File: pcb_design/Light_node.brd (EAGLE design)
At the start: 17.8 x 37.3 mm, 29 parts, among them IC1 ATmega328P, IC2 MIC5225-5v, Q1 reset, Y1 16MHz

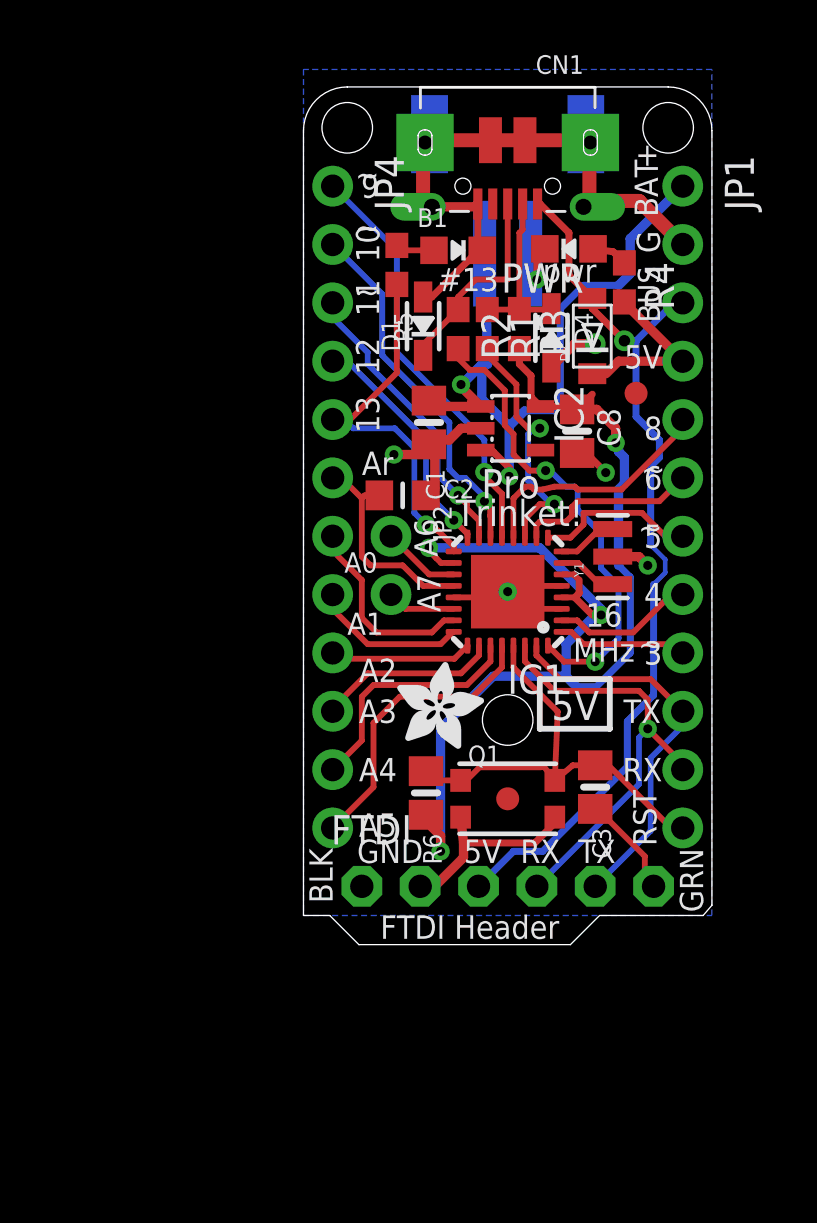
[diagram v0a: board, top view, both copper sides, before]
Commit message: Pulled the regulator components
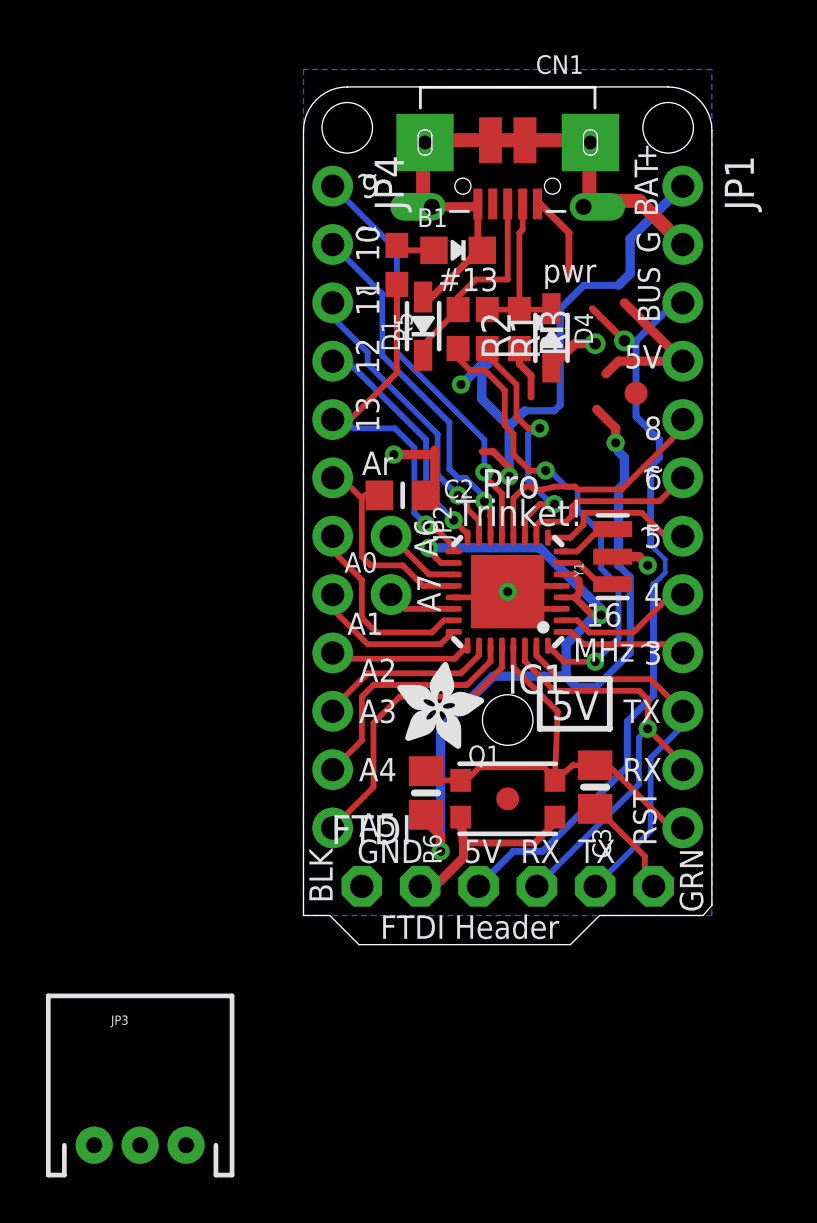
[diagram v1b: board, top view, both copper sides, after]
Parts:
- removed BAT: JST 2-PH, microbuilder:JSTPH2
- removed C1, C8: 10uF, microbuilder:0805-NO
- removed D2: SCHOTTKY, adafruit:SOD-123FL
- removed IC2: MIC5225-5v, adafruit:SOT23-5L
- removed PWR: green, microbuilder:CHIPLED_0805_NOOUTLINE
- removed R4: 470 (0603), microbuilder:0603-NO
- added JP3: (no value), SparkFun:JST-3-PTH
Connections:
- removed net N$6: PWR.A, R4.1
- net +5V: no longer C8.1, D2.C, IC2.5, R4.2
- net GND: no longer BAT.1, C1.2, C8.2, IC2.2, PWR.C
- net VBAT: no longer BAT.2, C1.1, IC2.1, IC2.3
- net VBUS: no longer D2.A
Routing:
- net VBAT: track 32.7 -> 24.3 mm
- net GND: track 58.0 -> 50.0 mm, vias 6 -> 4
- net +5V: track 60.2 -> 55.8 mm
- net VBUS: track 39.5 -> 37.6 mm
- net N$6: track 1.57 -> 0.00 mm

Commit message: added a bunch of new stuff in
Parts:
- removed JP2: (no value), microbuilder:1X02_ROUND
- removed JP4: (no value), adafruit:1X12-CB
- added B2: red, microbuilder:CHIPLED_0805_NOOUTLINE
- added C1, C4: 10µF, microbuilder:0805-NO
- added C5, C8: 10uF, microbuilder:0805-NO
- added CN2: JSTPH, microbuilder:JSTPH2
- added D2, D3: SCHOTTKY, adafruit:SOD-123FL
- added IC2: MIC5225-3.3v, adafruit:SOT23-5L
- added LED2: GREEN, microbuilder:CHIPLED_0805_NOOUTLINE
- added R4: 470 (0603), microbuilder:0603-NO
- added R8: 470, microbuilder:0805-NO
- added R9: 10K\, microbuilder:0805-NO
- added U1: MCP73831T-2ACI/OT, microbuilder:SOT23-5
- JP1: device adafruit:1X12-CB -> microbuilder:1X02_ROUND
- moved JP3 43.0 mm to (26.0, 4.00), turned to 180 degrees
- moved JP1 34.7 mm to (19.0, -15.0), turned to 0 degrees
- moved D4 12.0 mm to (13.7, 27.1)
- moved R3 11.8 mm to (12.1, 27.5)
- moved R1 11.7 mm to (10.6, 27.5)
- moved IC1 11.2 mm to (11.0, 16.1)
- moved U$7 11.2 mm to (6.17, 9.24)
- moved B1 11.2 mm to (8.84, 31.0)
- moved C3 11.2 mm to (14.8, 7.59)
- moved CN1 11.2 mm to (11.0, 33.8)
- moved FTDI 11.2 mm to (11.0, 3.27)
- moved Q1 11.2 mm to (11.0, 7.08)
- moved R2 11.2 mm to (8.84, 27.5)
- moved R6 11.2 mm to (7.44, 7.33)
- moved U$1 11.2 mm to (16.6, 24.7)
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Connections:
- new net +3V3: C8.1, IC2.5
- new net N$10: IC1.4, IC1.6
- new net N$4: B2.A, R4.1
- new net N$5: IC1.18
- new net N$6: R8.2, U1.1
- new net N$7: R9.1, U1.5
- new net N$8: LED2.A, R8.1
- new net N$9: C5.1, D2.C, D3.C, IC2.1, IC2.3
- new net STRIP_CNTRL: JP3.2
- net +5V: now also C1.1, CN1.VBUS, D2.A, JP1.1, R4.2, U1.4; no longer IC1.18, IC1.4, IC1.6, JP1.4, R6.2
- net A0: no longer JP4.7
- net A1: no longer JP4.8
- net A2: no longer JP4.9
- net A3: no longer JP4.10
- net A4: no longer JP4.11
- net A5: no longer JP4.12
- net A6: no longer JP2.1
- net A7: no longer JP2.2
- net AREF: no longer JP4.6
- net D10: no longer JP4.2
- net D11: no longer JP4.3
- net D12: no longer JP4.4
- net D13: no longer JP4.5
- net D3: no longer JP1.9
- net D4: no longer JP1.8
- net D5: no longer JP1.7
- net D6: no longer JP1.6
- net D8: no longer JP1.5
- net D9: no longer JP4.1
- net GND: now also B2.C, C1.2, C4.2, C5.2, C8.2, CN2.1, IC2.2, JP3.1, LED2.C, R9.2, U1.2; no longer JP1.2
- net RESET: no longer JP1.12
- net RXD: no longer JP1.11
- net TXD: no longer JP1.10
- net VBAT: now also C4.1, CN2.2, D3.A, JP1.2, JP3.3, U1.3; no longer JP1.1
- net VBUS: no longer CN1.VBUS, JP1.3
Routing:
- net VBAT: track 24.3 -> 0.00 mm, vias 2 -> 0
- net D13: track 17.0 -> 0.00 mm, vias 1 -> 0
- net D10: track 15.9 -> 0.00 mm, vias 1 -> 0
- net D11: track 13.2 -> 0.00 mm, vias 1 -> 0
- net A5: track 12.8 -> 0.00 mm
- net D8: track 10.9 -> 0.00 mm
- net A4: track 10.6 -> 0.00 mm
- net D12: track 10.5 -> 0.00 mm, vias 1 -> 0
- net AREF: track 9.52 -> 0.00 mm
- net A0: track 8.56 -> 0.00 mm
- net D6: track 7.99 -> 0.00 mm
- net A3: track 7.88 -> 0.00 mm
- net D5: track 7.04 -> 0.00 mm
- net A1: track 6.76 -> 0.00 mm
- net GND: track 50.0 -> 43.6 mm, vias 4 -> 3
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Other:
- board text removed: "+"
- board text removed: "-"
- board text removed: "10"
- board text removed: "11"
- board text removed: "12"
- board text removed: "13"
- board text removed: "3"
- board text removed: "4"
- board text removed: "5"
- board text removed: "6"
- board text removed: "8"
- board text removed: "9"
- board text removed: "A0"
- board text removed: "A1"
- board text removed: "A2"
- board text removed: "A3"
- board text removed: "A4"
- board text removed: "A5"
- board text removed: "Adafruit Pro Trinket ATmega328p 5V / 16MHz"
- board text removed: "Ar"
- board text removed: "BAT"
- board text removed: "BLK"
- board text removed: "BUS"
- board text removed: "G"
- board text removed: "GRN"
- board text removed: "Pro"
- board text removed: "RST"
- board text removed: "Trinket!"
- board text removed: "USBtinyISP or UNO FTDI Bootloader"
- board text removed: "VBat JST"
- board text removed: "VBat: 5-16VDC"
- board text removed: "~"

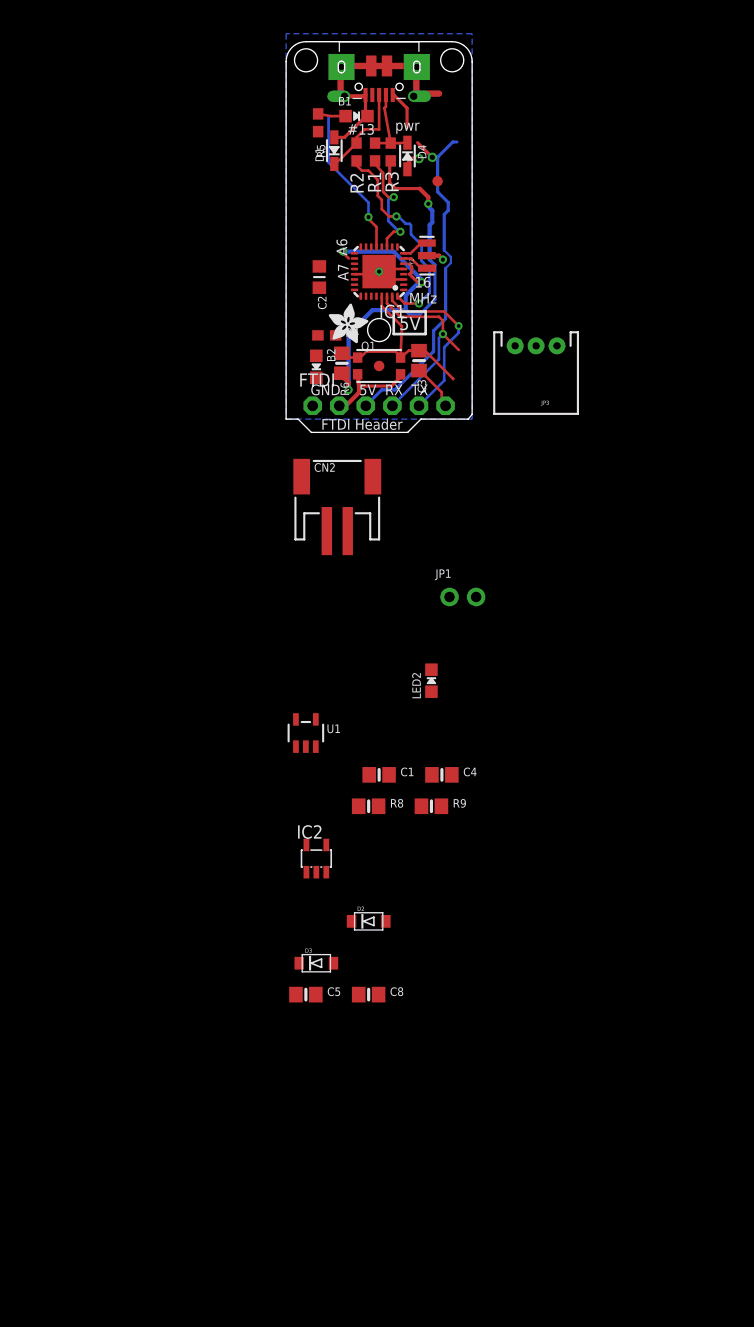
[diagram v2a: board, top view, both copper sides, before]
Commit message: jumpe us over to using the 3.3V version of the promicro
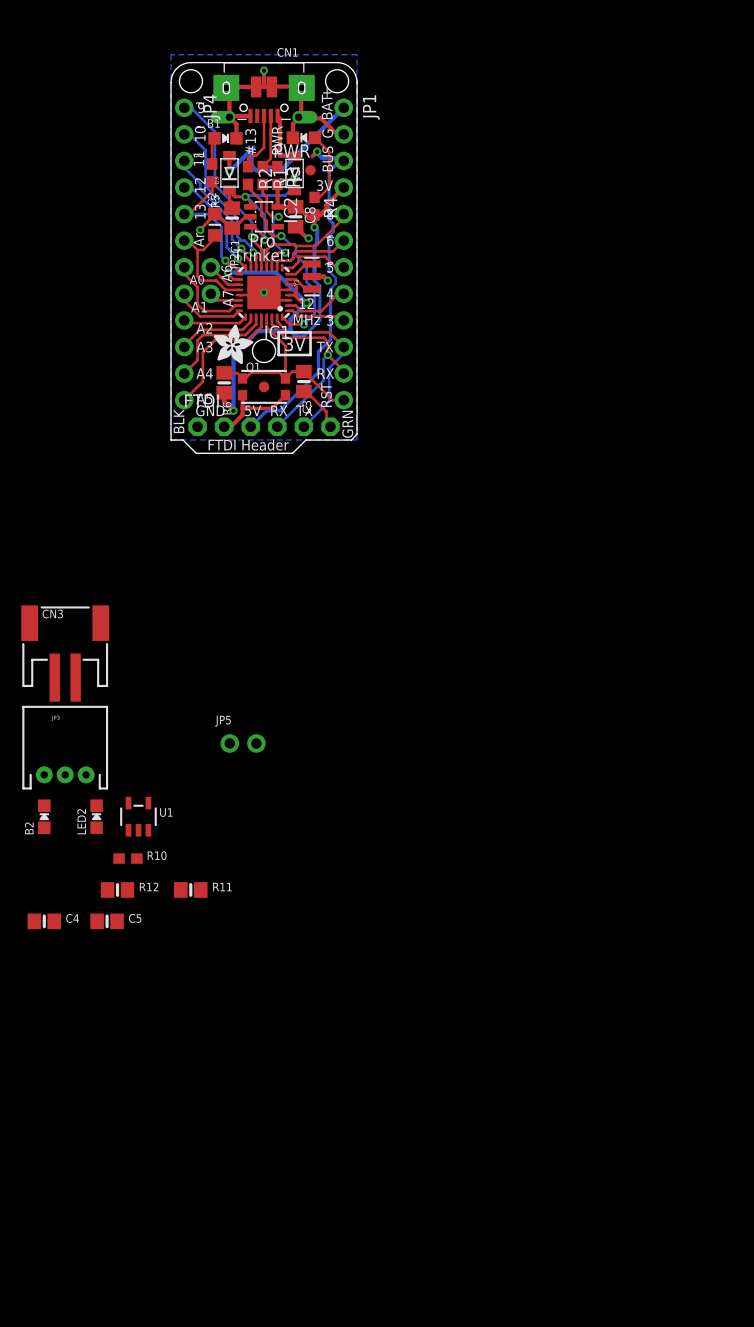
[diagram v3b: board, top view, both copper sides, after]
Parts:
- removed CN2: JSTPH, microbuilder:JSTPH2
- removed D1: 3.6v, microbuilder:SOD-323
- removed D4: 3.6V, microbuilder:SOD-323
- removed R8: 470, microbuilder:0805-NO
- removed R9: 10K\, microbuilder:0805-NO
- added CN3: JSTPH, microbuilder:JSTPH2
- added JP2, JP5: (no value), microbuilder:1X02_ROUND
- added JP4: (no value), adafruit:1X12-CB
- added PWR: green, microbuilder:CHIPLED_0805_NOOUTLINE
- added R10: 470 (0603), microbuilder:0603-NO
- added R11: 470, microbuilder:0805-NO
- added R12: 10K\, microbuilder:0805-NO
- C1: value 10µF -> 10uF
- C5: value 10uF -> 10µF
- JP1: device microbuilder:1X02_ROUND -> adafruit:1X12-CB
- R6: value 10K -> 10K (0603)
- Y1: value 16MHz -> 12MHz
- moved D3 76.0 mm to (-3.30, 25.5), turned to 90 degrees
- moved C8 74.7 mm to (3.02, 21.3), turned to 270 degrees
- moved D2 71.8 mm to (2.92, 25.5), turned to 90 degrees
- moved IC2 61.5 mm to (0.00, 21.3), turned to 270 degrees
- moved C1 55.0 mm to (-3.05, 21.2), turned to 270 degrees
- moved JP3 54.6 mm to (-19.0, -27.0), turned to 0 degrees
- moved B2 50.2 mm to (-21.0, -36.0), turned to 0 degrees
- moved C4 40.5 mm to (-21.0, -46.0)
- moved JP1 34.7 mm to (7.62, 17.8), turned to 270 degrees
- moved LED2 34.5 mm to (-16.0, -36.0)
- moved C5 20.2 mm to (-15.0, -46.0)
- moved U1 17.9 mm to (-12.0, -36.0)
- moved B1 12.7 mm to (-3.68, 28.8)
- moved R4 12.4 mm to (4.83, 22.4), turned to 270 degrees
- moved U$1 12.2 mm to (4.45, 25.8)
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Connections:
- removed net N$10: IC1.4, IC1.6
- net +3V3: now also IC1.18, IC1.4, IC1.6, JP1.4, R3.2, R4.2, R6.2
- net +5V: now also C4.1, JP5.1, R10.2; no longer C1.1, JP1.1, R3.2, R4.2
- net A0: now also JP4.7
- net A1: now also JP4.8
- net A2: now also JP4.9
- net A3: now also JP4.10
- net A4: now also JP4.11
- net A5: now also JP4.12
- net A6: now also JP2.1
- net A7: now also JP2.2
- net AREF: now also JP4.6
- net D+: no longer D1.C
- net D-: no longer D4.C
- net D10: now also JP4.2
- net D11: now also JP4.3
- net D12: now also JP4.4
- net D13: now also JP4.5
- net D3: now also JP1.9
- net D4: now also JP1.8
- net D5: now also JP1.7
- net D6: now also JP1.6
- net D8: now also JP1.5
- net D9: now also JP4.1
- net GND: now also CN3.1, JP1.2, PWR.C, R12.2; no longer CN2.1, D1.A, D4.A, R9.2
- net N$4: now also R10.1; no longer R4.1
- net N$5: now also R11.2, U1.1; no longer IC1.18
- net N$6: now also PWR.A, R4.1; no longer R8.2, U1.1
- net N$7: now also C1.1, D2.C, D3.C, IC2.1, IC2.3; no longer R9.1, U1.5
- net N$8: now also R12.1, U1.5; no longer LED2.A, R8.1
- net N$9: now also LED2.A, R11.1; no longer C5.1, D2.C, D3.C, IC2.1, IC2.3
- net RESET: now also JP1.12
- net RXD: now also JP1.11
- net TXD: now also JP1.10
- net VBAT: now also C5.1, CN3.2, JP1.1, JP5.2; no longer C4.1, CN2.2, JP1.2
- net VBUS: now also JP1.3
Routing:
- net +3V3: track 0.00 -> 55.7 mm, vias 0 -> 4
- net +5V: track 53.3 -> 5.00 mm, vias 4 -> 0
- net N$7: track 0.00 -> 19.6 mm, vias 0 -> 3
- net VBAT: track 0.00 -> 17.8 mm, vias 0 -> 1
- net D10: track 0.00 -> 16.1 mm, vias 0 -> 1
- net D13: track 0.00 -> 13.9 mm, vias 0 -> 1
- net D11: track 0.00 -> 13.2 mm, vias 0 -> 1
- net A5: track 0.00 -> 12.8 mm
- net AREF: track 0.00 -> 11.1 mm
- net D8: track 0.00 -> 10.8 mm
- net A4: track 0.00 -> 10.6 mm
- net D12: track 0.00 -> 10.5 mm, vias 0 -> 1
- net GND: track 43.6 -> 52.5 mm, vias 3 -> 5
- net A0: track 0.00 -> 8.56 mm
- net D6: track 0.00 -> 7.99 mm
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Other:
- outline, holes or cut-outs redrawn
- board text added: "+"
- board text added: "-"
- board text added: "10"
- board text added: "11"
- board text added: "12"
- board text added: "12 MHz"
- board text added: "13"
- board text added: "3"
- board text added: "3V"
- board text added: "4"
- board text added: "5"
- board text added: "6"
- board text added: "8"
- board text added: "9"
- board text added: "A0"
- board text added: "A1"
- board text added: "A2"
- board text added: "A3"
- board text added: "A4"
- board text added: "A5"
- board text added: "Adafruit Pro Trinket ATmega328p 3V / 12MHz"
- board text added: "Ar"
- board text added: "BAT"
- board text added: "BLK"
- board text added: "BUS"
- board text added: "G"
- board text added: "GRN"
- board text added: "PWR"
- board text added: "Pro"
- board text added: "RST"
- board text added: "Trinket!"
- board text added: "USBtinyISP or UNO FTDI Bootloader"
- board text added: "VBat JST"
- board text added: "VBat: 3.5-16VDC"
- board text added: "~"
- board text removed: "16 MHz"
- board text removed: "pwr"

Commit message: added in the accelerometer and removed the Reset pin
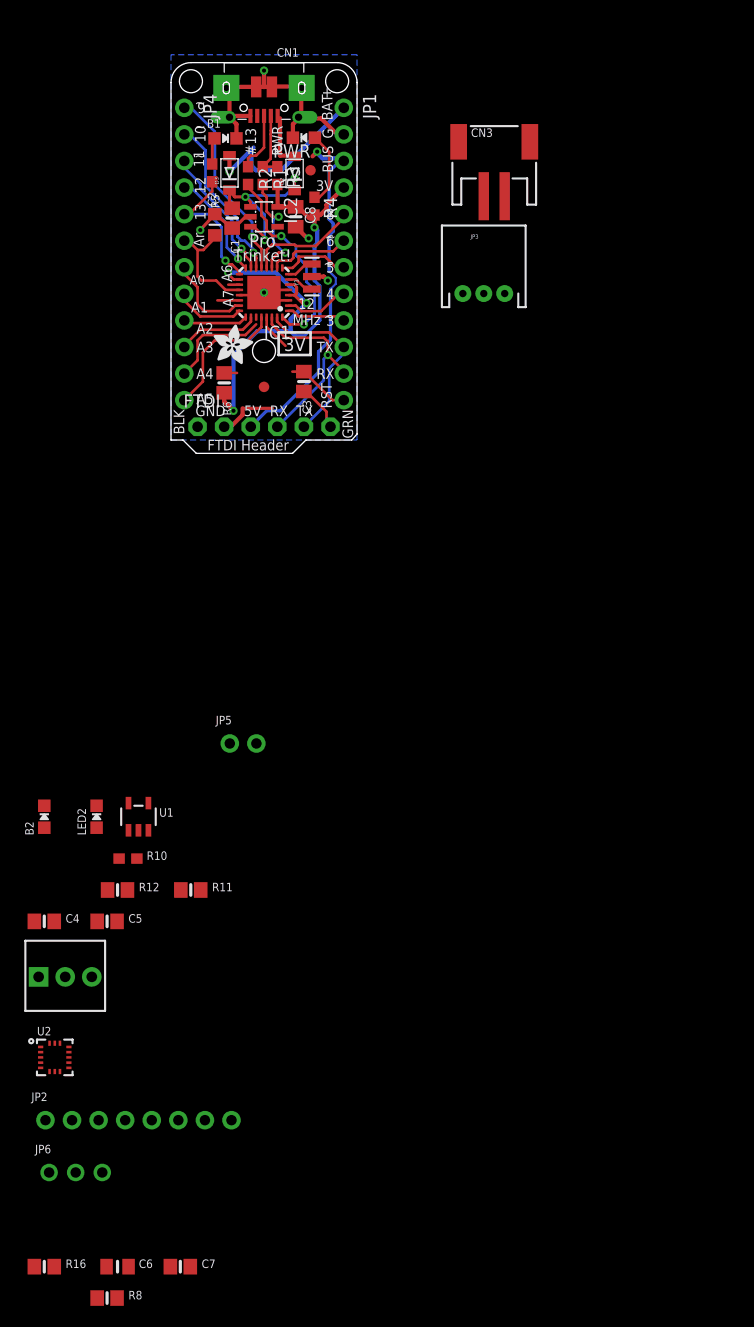
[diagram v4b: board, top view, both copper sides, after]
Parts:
- removed Q1: reset, microbuilder:BTN_KMR2_4.6X2.8
- added C6: 0.1uF, microbuilder:0805_10MGAP
- added C7: 10µF, microbuilder:0805-NO
- added JP6: (no value), microbuilder:1X03_ROUND
- added R16, R8: 10K, microbuilder:0805-NO
- added R7: TRIMPOT, SparkFun:3362U-2
- added U2: LIS3DHTR, microbuilder:LGA16_3X3MM
- JP2: device microbuilder:1X02_ROUND -> microbuilder:1X08_ROUND_70
- moved JP2 80.5 mm to (-12.0, -65.0), turned to 0 degrees
- moved CN3 61.6 mm to (22.0, 27.0)
- moved JP3 61.0 mm to (21.0, 19.0)
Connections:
- removed net A4: IC1.27, JP4.11
- removed net A5: IC1.28, JP4.12
- new net 3.3V: C6.1, C7.1, JP2.2, R8.2, U2.1, U2.14
- new net ADC1: JP6.1, U2.16
- new net ADC2: JP6.2, U2.15
- new net ADC3: JP6.3, U2.13
- new net CS: JP2.7, R8.1, U2.8
- new net INT1: JP2.8, U2.11
- new net SCL: IC1.28, JP2.4, JP4.12, U2.4
- new net SDA: IC1.27, JP2.5, JP4.11, U2.6
- new net SDO: JP2.6, R16.2, U2.7
- new net VIN: JP2.1
- net +3V3: now also R7.3
- net A6: now also R7.2; no longer JP2.1
- net A7: no longer JP2.2
- net GND: now also C6.2, C7.2, JP2.3, R16.1, R7.1, U2.10, U2.12, U2.5; no longer Q1.B, Q1.B'
- net RESET: no longer Q1.A, Q1.A'
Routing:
- net SCL: track 0.00 -> 12.8 mm
- net A5: track 12.8 -> 0.00 mm
- net A4: track 10.6 -> 0.00 mm
- net SDA: track 0.00 -> 9.94 mm
- net RESET: track 20.2 -> 10.8 mm
- net GND: track 52.5 -> 49.5 mm
- net A6: track 3.42 -> 1.07 mm
- net A7: track 2.99 -> 2.11 mm
